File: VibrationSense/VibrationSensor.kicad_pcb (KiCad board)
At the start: 2 copper layers, 40 x 58 mm, 11 parts, among them J101 Interface, U101 LIS2HH12

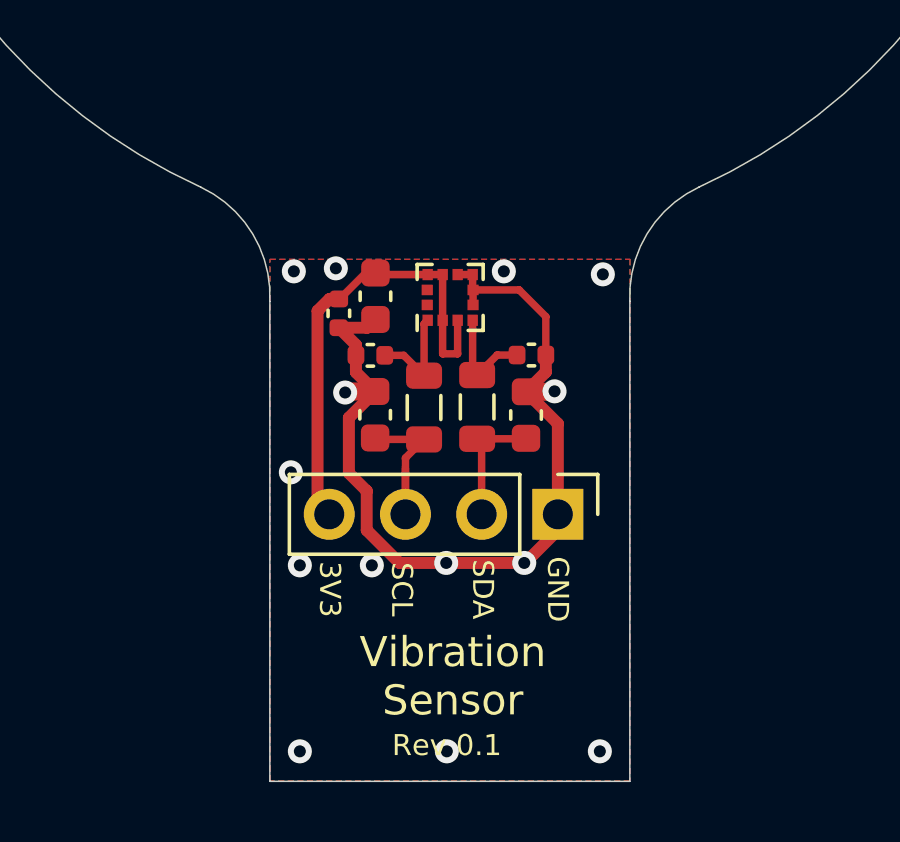
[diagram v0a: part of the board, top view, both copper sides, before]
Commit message: Change to LIS2DH12   (from HH).  DH has higher sampling rate, and is cheaper.
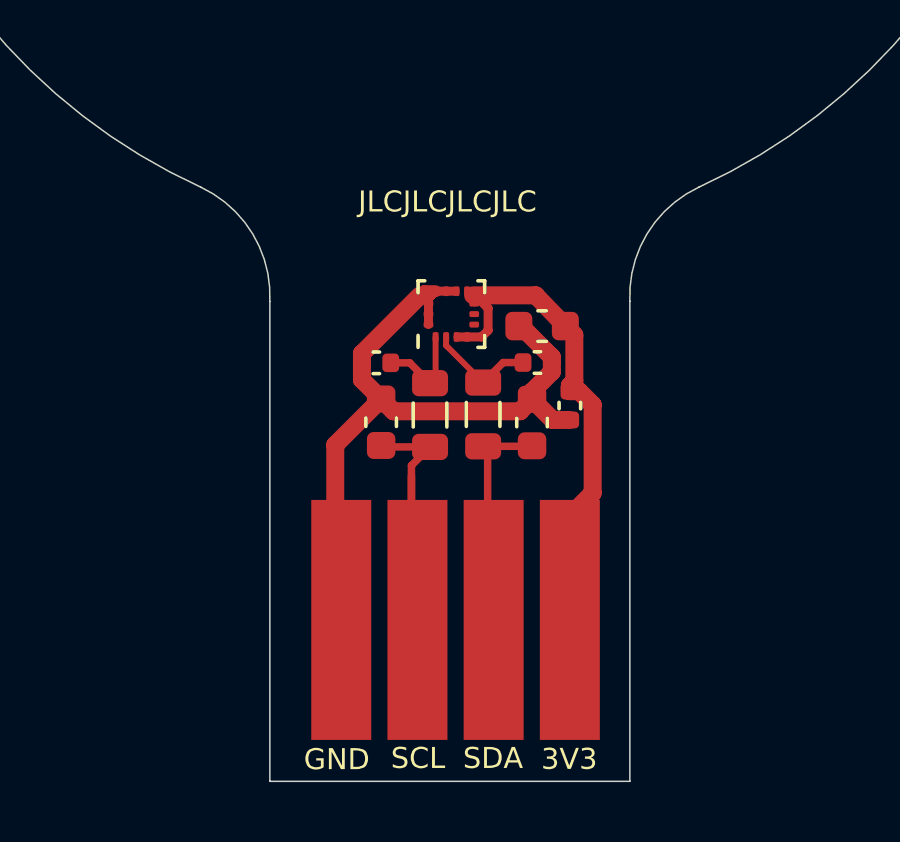
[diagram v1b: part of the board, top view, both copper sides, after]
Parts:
- J101: footprint Connector_PinHeader_2.54mm:PinHeader_1x04_P2.54mm_Vertical -> VibrationSense:Header_1x04_P2.54mm_SurfaceWires
- U101: value LIS2HH12 -> LIS2DH12TR; footprint Package_LGA:LGA-12_2x2mm_P0.5mm -> Package_LGA:LGA-14_2x2mm_P0.35mm_LayoutBorder3x4y
- moved C305 8.29 mm to (136.0, 97.5)
- moved C101 5.64 mm to (135.1, 94.8), turned to 0 degrees
- moved J101 3.54 mm to (136.0, 104.6)
- moved U101 0.56 mm to (132.1, 94.4)
- moved C102 0.32 mm to (134.7, 98.0)
- moved C103 0.32 mm to (129.7, 98.0)
- moved C105 0.32 mm to (129.6, 96.0)
- moved FB101 0.32 mm to (133.1, 97.8)
- moved FB102 0.32 mm to (131.3, 97.8)
- moved C104 0.32 mm to (134.9, 96.0)
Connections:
- J101 pad 1: GND -> +3V3
- J101 pad 4: +3V3 -> GND
- U101 pad 10: +3V3 -> GND
- U101 pad 11: (no net) -> GND
- U101 pad 12: (no net) -> GND
- U101 pad 2: +3V3 -> Net-(C104-Pad1)
- U101 pad 4: Net-(C104-Pad1) -> +3V3
- U101 pad 5: GND -> (no net)
- U101 pad 6: GND -> (no net)
- U101 pad 7: GND -> +3V3
- U101 pad 8: GND -> +3V3
- U101 pad 9: +3V3 -> GND
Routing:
- net GND: track 31.2 -> 21.8 mm, vias 14 -> 0
- net +3V3: track 15.9 -> 15.0 mm
- removed copper zone on B.Cu, net GND
- removed copper zone on F.Cu, net GND
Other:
- net class Default: clearance 0.2 -> 0.15
- rule trace_clearance: 0.2 -> 0.15
- board text added: "JLCJLCJLCJLC"
